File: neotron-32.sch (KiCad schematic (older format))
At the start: 18 parts

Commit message: Adding sub-sheets
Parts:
- removed C?: 100n, symbol Device:C
- removed J?: Conn_02x03_Odd_Even, symbol Connector_Generic:Conn_02x03_Odd_Even
- removed J?: SD_Card, symbol Connector:SD_Card
- removed J?: AudioJack3, symbol Connector:AudioJack3
- removed J?: DE9_Male_MountingHoles, symbol Connector:DB9_Male_MountingHoles
- removed J?: DB15_Female_HighDensity_MountingHoles, symbol Connector:DB15_Female_HighDensity_MountingHoles
- removed J? (x2): DB9_Female_MountingHoles, symbol Connector:DB9_Female_MountingHoles
- removed J? (x3): DIN-5_180degree, symbol Connector:DIN-5_180degree
- removed U?: ATtiny44-20PU, Package_DIP:DIP-14_W7.62mm, symbol MCU_Microchip_ATtiny:ATtiny44-20PU
- removed U?: 74LS245, symbol 74xx:74LS245
- removed U? (x5): 74LS125, symbol 74xx:74LS125
- added U?: TM4C123G_Launchpad, symbol TM4C_Launchpads:TM4C123G_Launchpad
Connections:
- net labels added: +3.3VP, PA2_SPI_CLK, PA3_SPI_CS0, PA4_SPI_MISO, PA5_SPI_MOSI, PA6_I2C_SCL, PA7_I2C_SDA, PB0_U1RX, PB1_U1TX, PB4_VGA_HSYNC, PB5_VGA_VSYNC, PB7_VGA_GREEN, PC4_U1RTS, PC5_U1CTS, PC6_MIDI_IN, PC7_MIDI_OUT, PD3_VGA_BLUE, PE0_U7RX, PE1_U7TX, PE4_AUDIO_L, PE5_AUDIO_R, PF1_VGA_RED, ~RESET
- net labels removed: AT_MISO, AT_MOSI, AT_RESET, AT_SCK, I2C1_SCL, I2C1_SDA, KB_CLK, KB_DAT, KB_IRQ, MS_CLK, MS_DAT
- wire segments 35 -> 68
- no-connect marks 0 -> 5
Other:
- note removed: "KEYBOARD/MOUSE CONTROLLER"
- note removed: "Place near Vcc"

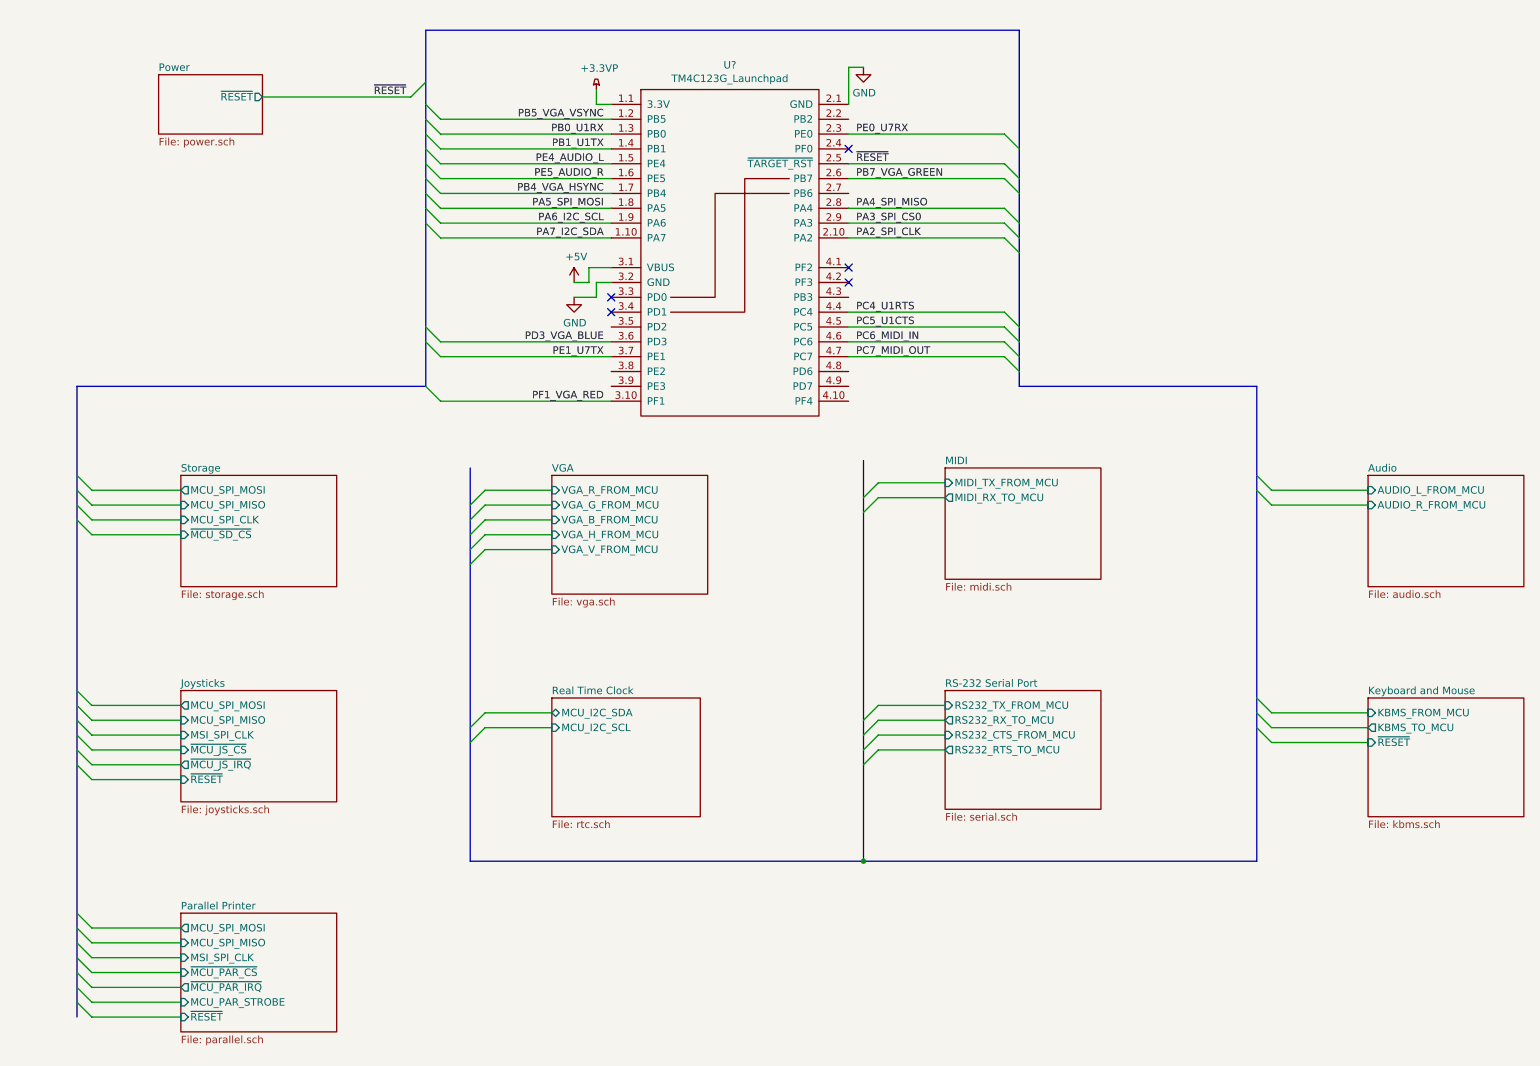
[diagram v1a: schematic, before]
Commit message: Added some footprints. Basic board outline.
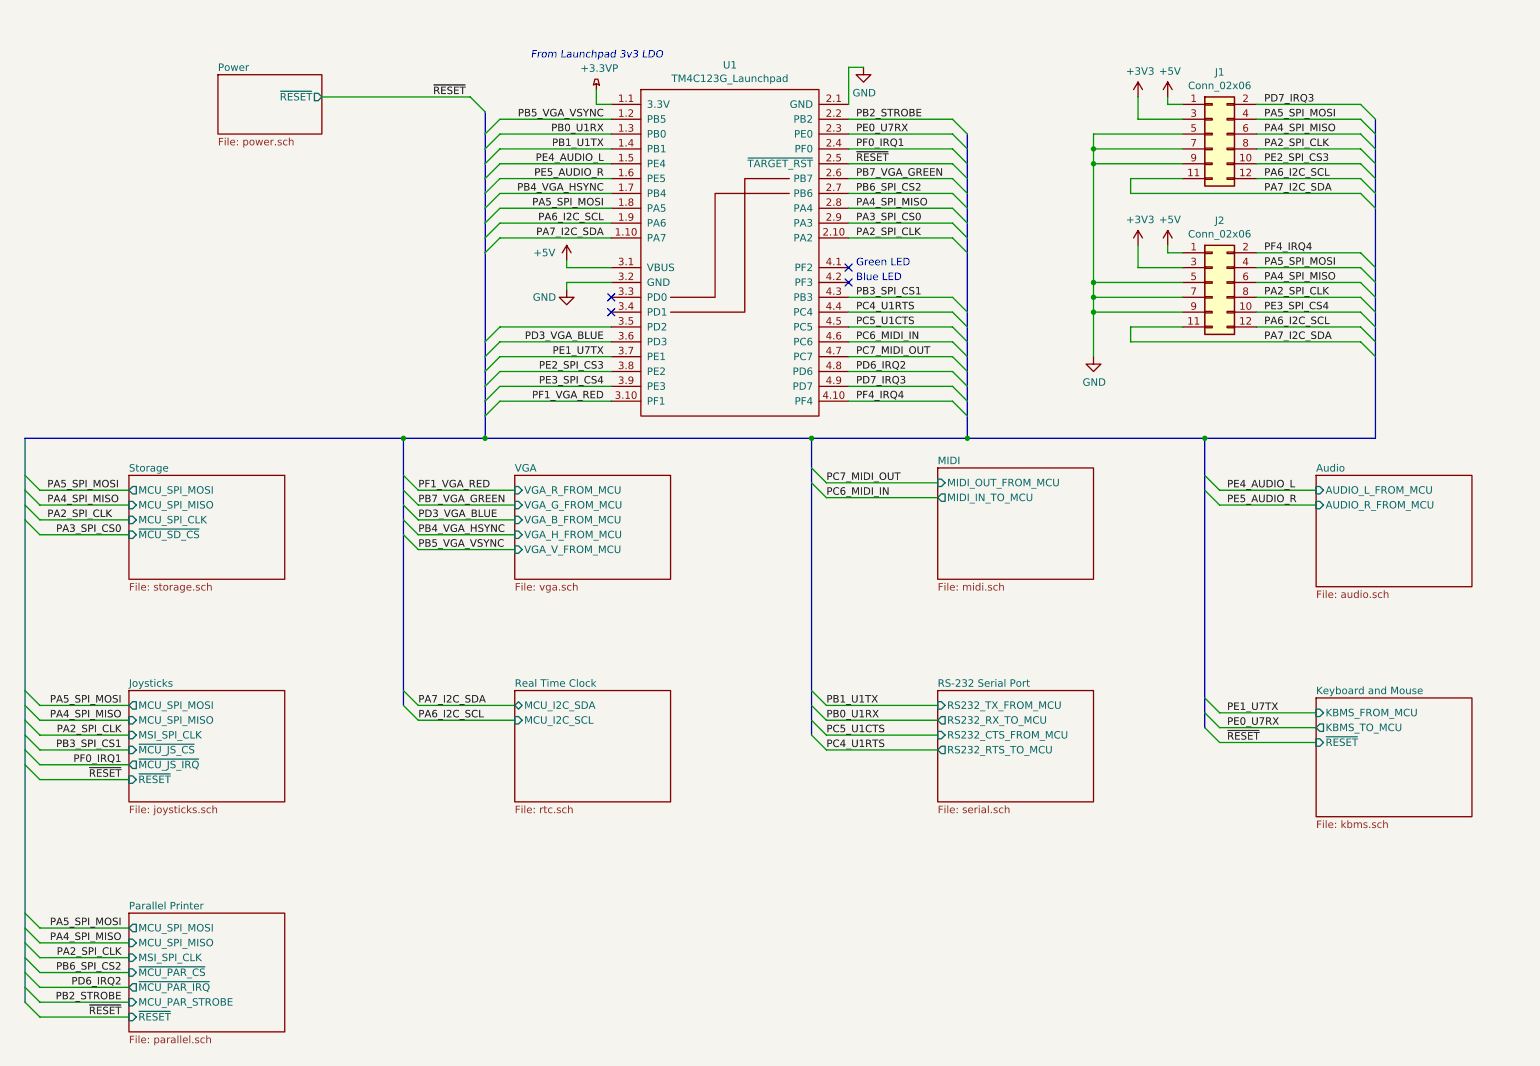
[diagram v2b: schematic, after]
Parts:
- added J1, J2: Conn_02x06, Connector_PinHeader_2.54mm:PinHeader_2x06_P2.54mm_Vertical, symbol Connector_Generic:Conn_02x06_Odd_Even
- U1: renamed from U?; footprint (none) -> JGP Footprints:Launchpad_4x10
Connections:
- net +5V: now also J1.1 (Pin_1), J2.1 (Pin_1)
- net GND: now also J1.5 (Pin_5), J1.7 (Pin_7), J1.9 (Pin_9), J2.5 (Pin_5), J2.7 (Pin_7), J2.9 (Pin_9)
- net PA2_SPI_CLK: now also J1.8 (Pin_8), J2.8 (Pin_8)
- net PA4_SPI_MISO: now also J1.6 (Pin_6), J2.6 (Pin_6)
- net PA5_SPI_MOSI: now also J1.4 (Pin_4), J2.4 (Pin_4)
- net PA6_I2C_SCL: now also J1.12 (Pin_12), J2.12 (Pin_12)
- net PA7_I2C_SDA: now also J1.11 (Pin_11), J2.11 (Pin_11)
- net PB2_STROBE: now reaches U1.2.2 (PB2)
- net PF0_IRQ1: now reaches U1.2.4 (PF0)
- net PB6_SPI_CS2: now reaches U1.2.7 (PB6)
- net PE2_SPI_CS3: now reaches U1.3.8 (PE2)
- net PE2_SPI_CS3: now also J1.10 (Pin_10)
- net PE3_SPI_CS4: now reaches U1.3.9 (PE3)
- net PE3_SPI_CS4: now also J2.10 (Pin_10)
- net PF4_IRQ4: now reaches U1.4.10 (PF4)
- net PF4_IRQ4: now also J2.2 (Pin_2)
- net PB3_SPI_CS1: now reaches U1.4.3 (PB3~)
- net PD6_IRQ2: now reaches U1.4.8 (PD6)
- net PD7_IRQ3: now reaches U1.4.9 (PD7)
- net PD7_IRQ3: now also J1.2 (Pin_2)
- new net +3V3: J1.3 (Pin_3), J2.3 (Pin_3)
- no-connect marks 5 -> 4
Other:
- note added: "Blue LED"
- note added: "From Launchpad 3v3 LDO"
- note added: "Green LED"

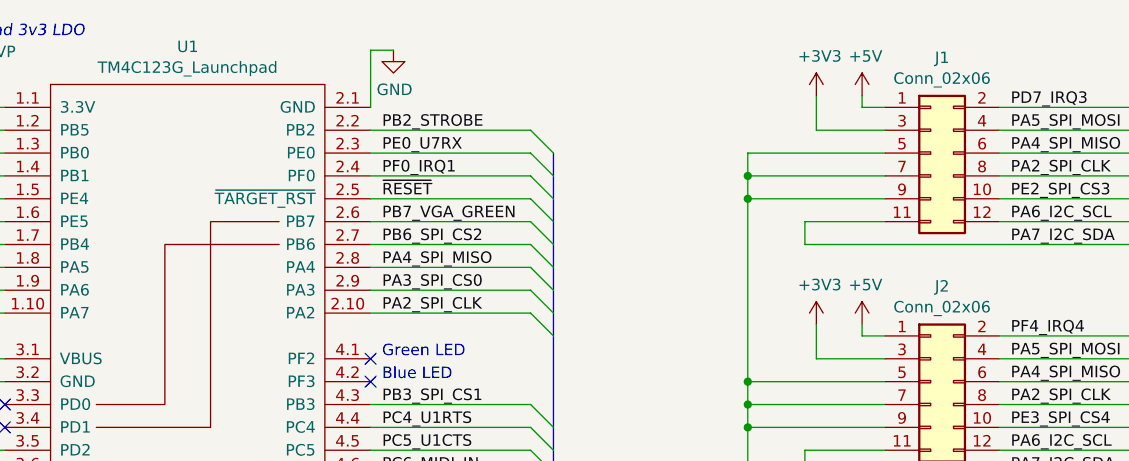
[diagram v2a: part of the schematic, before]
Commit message: Completed Power, SD, MIDI, Parallel and Joystick sheets.
Switch to sheet based 100x part numbering.
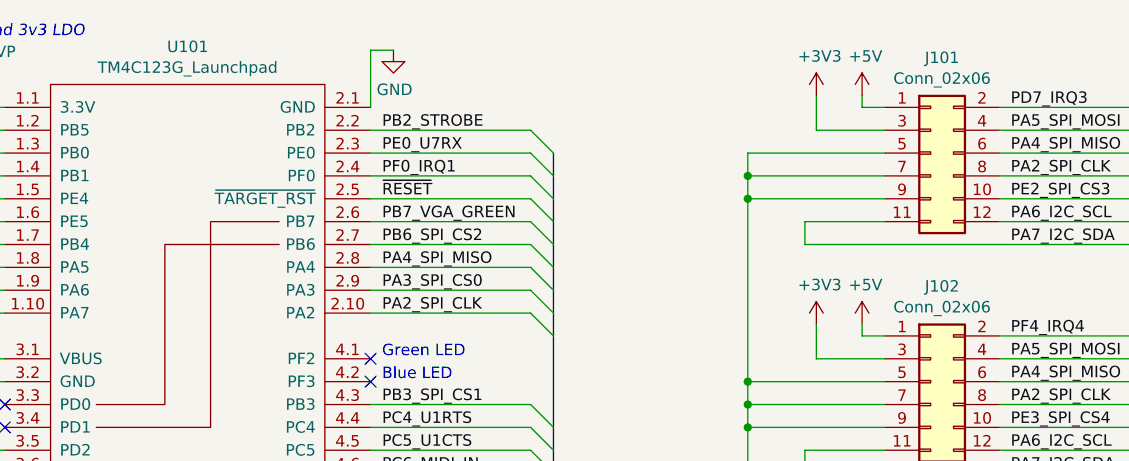
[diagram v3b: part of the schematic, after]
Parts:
- renumbered J1 to J101, J2 to J102, U1 to U101
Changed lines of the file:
@@
 $EndSheet
 $Comp
-L power:+3.3VP #PWR03
+L power:+3.3VP #PWR0103
 U 1 1 5DF729BF
 P 4800 1100
-F 0 "#PWR03" H 4950 1050 50  0001 C CNN
+F 0 "#PWR0103" H 4950 1050 50  0001 C CNN
 F 1 "+3.3VP" H 4820 1243 50  0000 C CNN
 F 2 "" H 4800 1100 50  0001 C CNN
@@
 	4800 1200 4800 1100
 $Comp
-L power:+5V #PWR01
+L power:+5V #PWR0101
 U 1 1 5DF73E13
 P 4600 2250
-F 0 "#PWR01" H 4600 2100 50  0001 C CNN
+F 0 "#PWR0101" H 4600 2100 50  0001 C CNN
 F 1 "+5V" H 4450 2300 50  0000 C CNN
 F 2 "" H 4600 2250 50  0001 C CNN
@@
 NoConn ~ 6500 2300
 $Comp
-L power:GND #PWR04
+L power:GND #PWR0104
 U 1 1 5DF75A3F
 P 6600 950
-F 0 "#PWR04" H 6600 700 50  0001 C CNN
+F 0 "#PWR0104" H 6600 700 50  0001 C CNN
 F 1 "GND" H 6605 777 50  0000 C CNN
 F 2 "" H 6600 950 50  0001 C CNN
@@
 	7200 1300 7300 1400
 $Comp
-L power:GND #PWR02
+L power:GND #PWR0102
 U 1 1 5DF745A3
 P 4600 2450
-F 0 "#PWR02" H 4600 2200 50  0001 C CNN
+F 0 "#PWR0102" H 4600 2200 50  0001 C CNN
 F 1 "GND" H 4450 2400 50  0000 C CNN
 F 2 "" H 4600 2450 50  0001 C CNN
@@
 PE3_SPI_CS4
 $Comp
-L Connector_Generic:Conn_02x06_Odd_Even J1
+L Connector_Generic:Conn_02x06_Odd_Even J101
 U 1 1 5DF61F52
 P 8950 1400
-F 0 "J1" H 9000 1817 50  0000 C CNN
+F 0 "J101" H 9000 1817 50  0000 C CNN
 F 1 "Conn_02x06" H 9000 1726 50  0000 C CNN
 F 2 "Connector_PinHeader_2.54mm:PinHeader_2x06_P2.54mm_Vertical" H 8950 1400 50  0001 C CNN
@@
 	8400 1800 8400 1700
 $Comp
-L Connector_Generic:Conn_02x06_Odd_Even J2
+L Connector_Generic:Conn_02x06_Odd_Even J102
 U 1 1 5DFAE92D
 P 8950 2400
-F 0 "J2" H 9000 2817 50  0000 C CNN
+F 0 "J102" H 9000 2817 50  0000 C CNN
 F 1 "Conn_02x06" H 9000 2726 50  0000 C CNN
 F 2 "Connector_PinHeader_2.54mm:PinHeader_2x06_P2.54mm_Vertical" H 8950 2400 50  0001 C CNN
@@
 	8400 2800 8400 2700
 $Comp
-L power:+5V #PWR08
+L power:+5V #PWR0108
 U 1 1 5DFBE594
 P 8650 1150
-F 0 "#PWR08" H 8650 1000 50  0001 C CNN
+F 0 "#PWR0108" H 8650 1000 50  0001 C CNN
 F 1 "+5V" H 8665 1323 50  0000 C CNN
 F 2 "" H 8650 1150 50  0001 C CNN
@@
 $EndComp
 $Comp
-L power:+3V3 #PWR06
+L power:+3V3 #PWR0106
 U 1 1 5DFBEDCD
 P 8450 1150
-F 0 "#PWR06" H 8450 1000 50  0001 C CNN
+F 0 "#PWR0106" H 8450 1000 50  0001 C CNN
 F 1 "+3V3" H 8465 1323 50  0000 C CNN
 F 2 "" H 8450 1150 50  0001 C CNN
@@
 $EndComp
 $Comp
-L power:GND #PWR05
+L power:GND #PWR0105
 U 1 1 5DFBF393
 P 8150 2900
-F 0 "#PWR05" H 8150 2650 50  0001 C CNN
+F 0 "#PWR0105" H 8150 2650 50  0001 C CNN
 F 1 "GND" H 8155 2727 50  0000 C CNN
 F 2 "" H 8150 2900 50  0001 C CNN
@@
 	8150 1600 8150 2400
 $Comp
-L power:+5V #PWR09
+L power:+5V #PWR0109
 U 1 1 5DFF5FD3
 P 8650 2150
-F 0 "#PWR09" H 8650 2000 50  0001 C CNN
+F 0 "#PWR0109" H 8650 2000 50  0001 C CNN
 F 1 "+5V" H 8665 2323 50  0000 C CNN
 F 2 "" H 8650 2150 50  0001 C CNN
@@
 	8450 2300 8450 2150
 $Comp
-L power:+3V3 #PWR07
+L power:+3V3 #PWR0107
 U 1 1 5E00E65B
 P 8450 2150
-F 0 "#PWR07" H 8450 2000 50  0001 C CNN
+F 0 "#PWR0107" H 8450 2000 50  0001 C CNN
 F 1 "+3V3" H 8465 2323 50  0000 C CNN
 F 2 "" H 8450 2150 50  0001 C CNN
@@
 	4900 2100 4150 2100
 $Comp
-L TM4C_Launchpads:TM4C123G_Launchpad U1
+L TM4C_Launchpads:TM4C123G_Launchpad U101
 U 1 1 5DF69932
 P 5700 2200
-F 0 "U1" H 5700 3465 50  0000 C CNN
+F 0 "U101" H 5700 3465 50  0000 C CNN
 F 1 "TM4C123G_Launchpad" H 5700 3374 50  0000 C CNN
 F 2 "JGP Footprints:Launchpad_4x10" H 5700 2200 50  0001 C CNN
